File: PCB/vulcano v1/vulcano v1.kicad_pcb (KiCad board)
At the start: 2 copper layers, 4 parts, among them J1 Screw_Terminal_01x02, J2 Screw_Terminal_01x02, J3 conector t, U1 DOIT-ESP32-DEVKIT-V1

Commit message: placa principal
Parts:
- added A1: Arduino_UNO_R2, Module:Arduino_UNO_R2, B.Cu at (210.4, 77.6)
- added C1: 0.33uF, Capacitor_THT:C_Disc_D4.3mm_W1.9mm_P5.00mm, F.Cu at (49.7, 60.8)
- added C2: 0.1uF, Capacitor_THT:C_Disc_D4.3mm_W1.9mm_P5.00mm, F.Cu at (49.7, 72.9)
- added C3: 0.33uF, Capacitor_THT:C_Disc_D4.3mm_W1.9mm_P5.00mm, F.Cu at (58.6, 72.9)
- added C4: 0.1uF, Capacitor_THT:C_Disc_D4.3mm_W1.9mm_P5.00mm, F.Cu at (58.6, 60.7)
- added D1: 1N4007, Diode_THT:D_DO-41_SOD81_P10.16mm_Horizontal, F.Cu at (67.2, 77.1)
- added J4: Conn_02x05_Counter_Clockwise, Connector_IDC:IDC-Header_2x05_P2.54mm_Vertical, F.Cu at (138.1, 60.9)
- added J5: Conn_01x05_Pin, Connector_PinSocket_2.54mm:PinSocket_1x05_P2.54mm_Vertical, F.Cu at (117.2, 60.9)
- added J6: Conn_01x05_Pin, Connector_PinSocket_2.54mm:PinSocket_1x05_P2.54mm_Vertical, F.Cu at (121.1, 60.9)
- added J7: Conn_01x06_Pin, Connector_PinSocket_2.54mm:PinSocket_1x06_P2.54mm_Vertical, F.Cu at (136.8, 44.8)
- added J8: Conn_01x06_Pin, Connector_PinSocket_2.54mm:PinSocket_1x06_P2.54mm_Vertical, F.Cu at (136.8, 50.8)
- added Q1: BC547, Package_TO_SOT_THT:TO-92_Wide, F.Cu at (119.7, 68.8)
- added Q2: BC547, Package_TO_SOT_THT:TO-92_Wide, F.Cu at (131.7, 80.9)
- added Q3: BC547, Package_TO_SOT_THT:TO-92_Wide, F.Cu at (131.4, 67.4)
- added Q4: BC547, Package_TO_SOT_THT:TO-92_Wide, F.Cu at (116.2, 44.7)
- added Q5: BC547, Package_TO_SOT_THT:TO-92_Wide, F.Cu at (119.7, 81.3)
- added R12: 4k7, Resistor_THT:R_Axial_DIN0204_L3.6mm_D1.6mm_P7.62mm_Horizontal, F.Cu at (127.5, 45.0)
- added R15: 4k7, Resistor_THT:R_Axial_DIN0204_L3.6mm_D1.6mm_P7.62mm_Horizontal, F.Cu at (121.7, 87.8)
- added R3: 4k7, Resistor_THT:R_Axial_DIN0204_L3.6mm_D1.6mm_P7.62mm_Horizontal, F.Cu at (121.6, 74.0)
- added R6: 4k7, Resistor_THT:R_Axial_DIN0204_L3.6mm_D1.6mm_P7.62mm_Horizontal, F.Cu at (136.8, 86.4)
- added R9: 4k7, Resistor_THT:R_Axial_DIN0204_L3.6mm_D1.6mm_P7.62mm_Horizontal, F.Cu at (136.4, 73.5)
- added SW1: SW_SPDT, Button_Switch_THT:SW_CuK_JS202011CQN_DPDT_Straight, F.Cu at (69.5, 60.7)
- added U2: LM7809_TO220, Package_TO_SOT_THT:TO-220-3_Vertical, F.Cu at (53.6, 64.3)
- added U3: LM7806_TO220, Package_TO_SOT_THT:TO-220-3_Vertical, F.Cu at (64.0, 69.3)
- J1: footprint Connector_AMASS:AMASS_XT60-F_1x02_P7.20mm_Vertical -> TerminalBlock:TerminalBlock_bornier-2_P5.08mm
- J2: moved to F.Cu
- J3: value conector t -> Screw_Terminal_01x02; footprint Connector_AMASS:AMASS_XT60-F_1x02_P7.20mm_Vertical -> TerminalBlock:TerminalBlock_bornier-2_P5.08mm
- moved J2 129.6 mm to (60.0, 53.9), turned to 180 degrees
- moved J1 98.9 mm to (74.5, 53.8), turned to 180 degrees
- moved J3 91.3 mm to (72.0, 69.5)
- moved U1 43.2 mm to (95.0, 48.3)
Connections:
- net Net-(J1-Pin_2) renamed +12V
- J1 pad 1: GND -> Net-(J1-Pin_1)
- J2 pad 2: VCC -> GND
- U1 pad 10: unconnected-(U1-GPIO27_ADC2-CH7_RTC-GPIO17-Pad10) -> PWMA
- U1 pad 11: unconnected-(U1-GPIO14_ADC2-CH6_HSPI-CLK_RTC-GPIO16-Pad11) -> BIN1
- U1 pad 17: unconnected-(U1-GND-Pad17) -> GND
- U1 pad 18: unconnected-(U1-VIN-Pad18) -> +5V
- U1 pad 19: unconnected-(U1-3V3-Pad19) -> +3.3V
- U1 pad 20: unconnected-(U1-GPIO6_SCK/CLK-Pad20) -> X_SHUT_2
- U1 pad 21: unconnected-(U1-GPIO7_SDO/SD0-Pad21) -> X_SHUT_1
- U1 pad 26: unconnected-(U1-GPIO4_ADC2-CH0_RTC-GPIO10-Pad26) -> SENSOR_5_PIN
- U1 pad 29: unconnected-(U1-GPIO5_VSPI-CS0-Pad29) -> SENSOR_2_PIN
- U1 pad 30: unconnected-(U1-GPIO18_VSPI-CLK-Pad30) -> SENSOR_1_PIN
- U1 pad 31: unconnected-(U1-GPIO19_VSPI-MISO-Pad31) -> SENSOR_3_PIN
- U1 pad 32: unconnected-(U1-GPIO21_I2C-SDA-Pad32) -> SDA
- U1 pad 35: unconnected-(U1-GPIO22_I2C-SCL-Pad35) -> SCL
- U1 pad 36: unconnected-(U1-GPIO23_VSPI-MOSI-Pad36) -> SENSOR_4_PIN
- U1 pad 6: unconnected-(U1-GPIO32_ADC1-CH4_RTC-GPIO9-Pad6) -> BIN2
- U1 pad 7: unconnected-(U1-GPIO33_ADC1-CH5_RTC-GPIO8-Pad7) -> AIN2
- U1 pad 8: unconnected-(U1-GPIO25_ADC2-CH8_DAC1_RTC-GPIO6-Pad8) -> AIN1
- U1 pad 9: unconnected-(U1-GPIO26_ADC2-CH9_DAC2_RTC-GPIO7-Pad9) -> PWMB
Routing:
- net GND: track 0.00 -> 461.8 mm, vias 0 -> 2
- net +5V: track 0.00 -> 305.7 mm, vias 0 -> 4
- net BIN1: track 0.00 -> 209.2 mm
- net PWMA: track 0.00 -> 194.2 mm
- net PWMB: track 0.00 -> 182.2 mm
- net AIN1: track 0.00 -> 171.1 mm
- net AIN2: track 0.00 -> 160.4 mm
- net BIN2: track 0.00 -> 148.7 mm
- net +3.3V: track 0.00 -> 127.7 mm
- net RX_1: track 0.00 -> 81.3 mm, vias 0 -> 2
- net X_SHUT_1: track 0.00 -> 64.0 mm, vias 0 -> 2
- net X_SHUT_2: track 0.00 -> 40.1 mm, vias 0 -> 2
- net +12V: track 0.00 -> 37.9 mm
- net Sensores: track 0.00 -> 36.4 mm
- net Sensores_2: track 0.00 -> 32.9 mm
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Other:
- board outline added: 180 x 80 mm

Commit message: pcb vulcano terminada (reviasala ana)
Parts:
- removed SW1: SW_SPDT, Button_Switch_THT:SW_CuK_JS202011CQN_DPDT_Straight
- added BZ1: Buzzer, Buzzer_Beeper:MagneticBuzzer_Kingstate_KCG0601, F.Cu at (100.6, 52.6)
- added C5: C_Polarized_US, Capacitor_THT:CP_Radial_D8.0mm_P5.00mm, F.Cu at (76.8, 52.8)
- added J10: Conn_01x03_Pin, Connector_PinHeader_2.54mm:PinHeader_1x03_P2.54mm_Vertical, F.Cu at (76.1, 81.3)
- added J11: Conn_01x06_Pin, Connector_PinHeader_2.54mm:PinHeader_1x06_P2.54mm_Vertical, F.Cu at (87.4, 46.7)
- added J9: Conn_01x05_Pin, Connector_PinHeader_2.54mm:PinHeader_1x05_P2.54mm_Vertical, F.Cu at (49.3, 81.4)
- added Q6: BC547, Package_TO_SOT_THT:TO-92_Wide, F.Cu at (102.4, 56.1)
- added R1: 4k7, Resistor_THT:R_Axial_DIN0204_L3.6mm_D1.6mm_P7.62mm_Horizontal, F.Cu at (177.3, 110.2)
- added R2: 4k7, Resistor_THT:R_Axial_DIN0204_L3.6mm_D1.6mm_P7.62mm_Horizontal, F.Cu at (105.0, 71.1)
- added REF**: MountingHole_3.2mm_M3, MountingHole:MountingHole_3.2mm_M3, F.Cu at (48.5, 42.0)
- added REF**: MountingHole_3.2mm_M3, MountingHole:MountingHole_3.2mm_M3, F.Cu at (209.2, 109.1)
- added SW2: SW_Push, Button_Switch_THT:SW_PUSH_6mm, F.Cu at (59.3, 101.3)
- J1, J3: footprint TerminalBlock:TerminalBlock_bornier-2_P5.08mm -> deans:DEANS
- J2: footprint Connector_AMASS:AMASS_XT60-F_1x02_P7.20mm_Vertical -> Connector_AMASS:AMASS_XT60-M_1x02_P7.20mm_Vertical
- moved J3 25.6 mm to (69.6, 44.0), turned to -90 degrees
- moved J1 7.48 mm to (70.4, 60.0), turned to -135 degrees
- moved Q4 3.34 mm to (115.2, 47.9)
- moved J2 3.07 mm to (57.0, 53.9), turned to 90 degrees
- moved R12 2.29 mm to (127.6, 47.3)
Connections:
- A1 pad 5: +5V -> +3.3V
- J1 pad 1: Net-(J1-Pin_1) -> VCC
- U1 pad 13: unconnected-(U1-GPIO13_ADC2-CH4_HSPI-MOSI_RTC-GPIO14-Pad13) -> DI
- U1 pad 14: unconnected-(U1-GPIO9_SHD/SD2-Pad14) -> SW
- U1 pad 15: unconnected-(U1-GPIO10_SWP/SD3-Pad15) -> DT
- U1 pad 16: unconnected-(U1-GPIO11_CSC/CMD-Pad16) -> CLK
- U1 pad 2: unconnected-(U1-GPIO36_ADC-CH0_SENS-VP_RTC-GPIO0-Pad2) -> CNY_1
- U1 pad 20: X_SHUT_2 -> unconnected-(U1-GPIO6_SCK/CLK-Pad20)
- U1 pad 22: unconnected-(U1-GPIO8_SDI/SD1-Pad22) -> X_SHUT_2
- U1 pad 25: unconnected-(U1-GPIO2_ADC2-CH2_RTC-GPIO12-Pad25) -> CNY_4
- U1 pad 28: unconnected-(U1-GPIO17_UART2-TX-Pad28) -> buzzer
- U1 pad 3: unconnected-(U1-GPIO39_ADC1-CH3_SENS-VN_RTC-GPIO3-Pad3) -> CNY_2
- U1 pad 4: unconnected-(U1-GPIO34_ADC1-CH6_RTC-GPIO4-Pad4) -> CNY_3
- U1 pad 5: unconnected-(U1-GPIO35_ADC1-CH7_RTC-GPIO5-Pad5) -> INIT
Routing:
- net +3.3V: track 127.7 -> 489.5 mm, vias 0 -> 4
- net INIT: track 0.00 -> 167.0 mm, vias 0 -> 2
- net GND: track 461.8 -> 553.8 mm
- net +5V: track 305.7 -> 224.7 mm, vias 4 -> 6
- net BIN1: track 209.2 -> 253.2 mm
- net CNY_4: track 0.00 -> 39.8 mm
- net SW: track 0.00 -> 34.1 mm, vias 0 -> 2
- net DT: track 0.00 -> 34.1 mm, vias 0 -> 2
- net CLK: track 0.00 -> 34.1 mm, vias 0 -> 2
- net CNY_3: track 0.00 -> 21.1 mm
- net CNY_2: track 0.00 -> 16.0 mm
- net VCC: track 8.77 -> 22.2 mm
- net CNY_1: track 0.00 -> 11.3 mm
- net Net-(BZ1--): track 0.00 -> 10.8 mm
- net Net-(J1-Pin_1): track 10.3 -> 0.00 mm
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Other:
- board size 180 x 80 mm -> 170.8 x 76.5 mm

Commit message: pdf atemga
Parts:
- moved J9 2.20 mm to (50.5, 83.2)
- moved R9 1.73 mm to (136.4, 71.7)
- moved Q3 1.39 mm to (131.5, 66.0)
- moved Q5 1.32 mm to (119.6, 82.6)
- moved R12 1.23 mm to (127.6, 46.1)
- moved R6 0.66 mm to (136.8, 87.1)
- moved Q2 0.66 mm to (131.7, 81.6)
- moved J10 0.40 mm to (76.2, 80.9)
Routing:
- net GND: track 553.8 -> 534.7 mm
- net +3.3V: track 489.5 -> 472.7 mm
- net BIN1: track 253.2 -> 257.4 mm
- net BIN2: track 146.5 -> 142.7 mm
- net +5V: track 224.7 -> 221.5 mm
- net AIN2: track 157.0 -> 153.8 mm
- net AIN1: track 167.5 -> 165.1 mm
- net Sensores_3: track 13.3 -> 11.6 mm
- net RX: track 23.1 -> 21.6 mm
- net PWMB: track 176.8 -> 175.4 mm
- net INIT: track 167.0 -> 165.7 mm
- net Sensores: track 36.4 -> 35.2 mm
- net PWMA: track 187.4 -> 186.4 mm
- net VCC: track 22.2 -> 21.2 mm
- net SDA: track 15.5 -> 14.6 mm
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
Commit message: placa central lista
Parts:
- C5: footprint Capacitor_THT:CP_Radial_D8.0mm_P5.00mm -> Capacitor_THT:CP_Radial_D13.0mm_P5.00mm
- moved J2 9.43 mm to (53.4, 62.7)
- moved C1 9.08 mm to (50.0, 69.8)
- moved C2 9.08 mm to (50.0, 82.0)
- moved C3 9.08 mm to (58.9, 82.0)
- moved U3 9.08 mm to (64.3, 78.4)
- moved C4 9.08 mm to (58.9, 69.8)
- moved U2 9.08 mm to (53.9, 73.4)
- moved J9 7.63 mm to (50.0, 90.8)
- moved J1 6.78 mm to (69.9, 66.8), turned to -90 degrees
- moved C5 6.72 mm to (70.7, 55.6)
- moved J3 6.10 mm to (63.5, 44.0)
- moved D1 5.96 mm to (69.5, 82.6)
- moved SW2 2.78 mm to (60.0, 104.0)
- moved J10 1.41 mm to (77.6, 80.9)
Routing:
- net (no net): track 0.73 -> 25.6 mm
- net +5V: track 221.5 -> 235.4 mm
- net PWMA: track 186.4 -> 195.0 mm
- net GND: track 534.7 -> 540.6 mm
- net PWMB: track 175.4 -> 181.1 mm
- net +3.3V: track 472.7 -> 467.3 mm
- net VCC: track 21.2 -> 25.6 mm
- net BIN1: track 257.4 -> 261.5 mm
- net CLK: track 33.7 -> 37.7 mm
- net DT: track 33.7 -> 37.3 mm
- net SW: track 33.7 -> 37.3 mm
- net AIN1: track 165.1 -> 168.3 mm
- net +12V: track 31.9 -> 29.7 mm
- net DI: track 6.72 -> 4.90 mm
- net BIN2: track 142.7 -> 141.7 mm
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
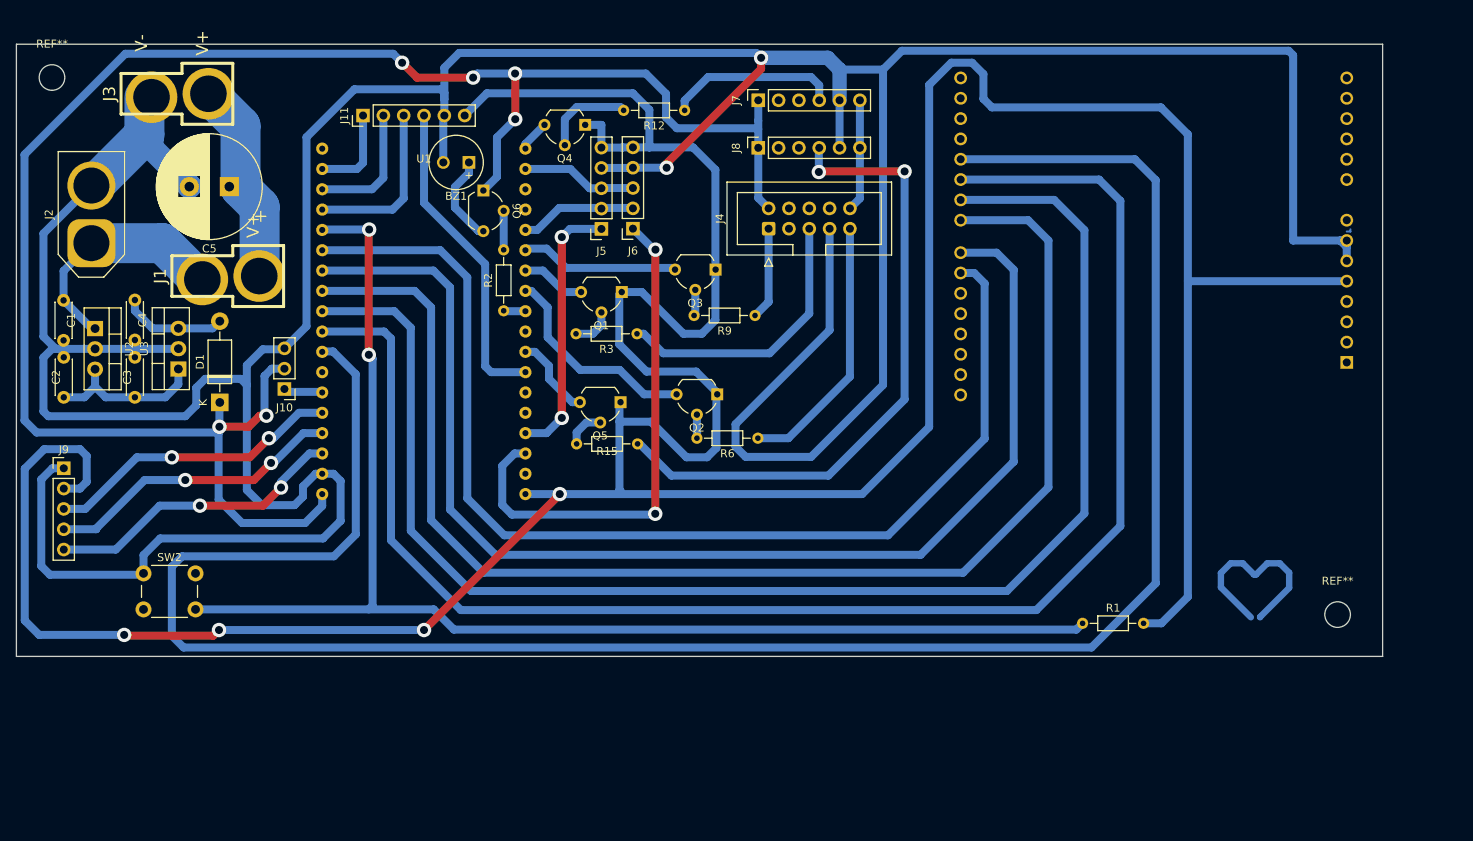
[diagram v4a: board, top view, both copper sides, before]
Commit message: placa vulcano falta indicar tornillos
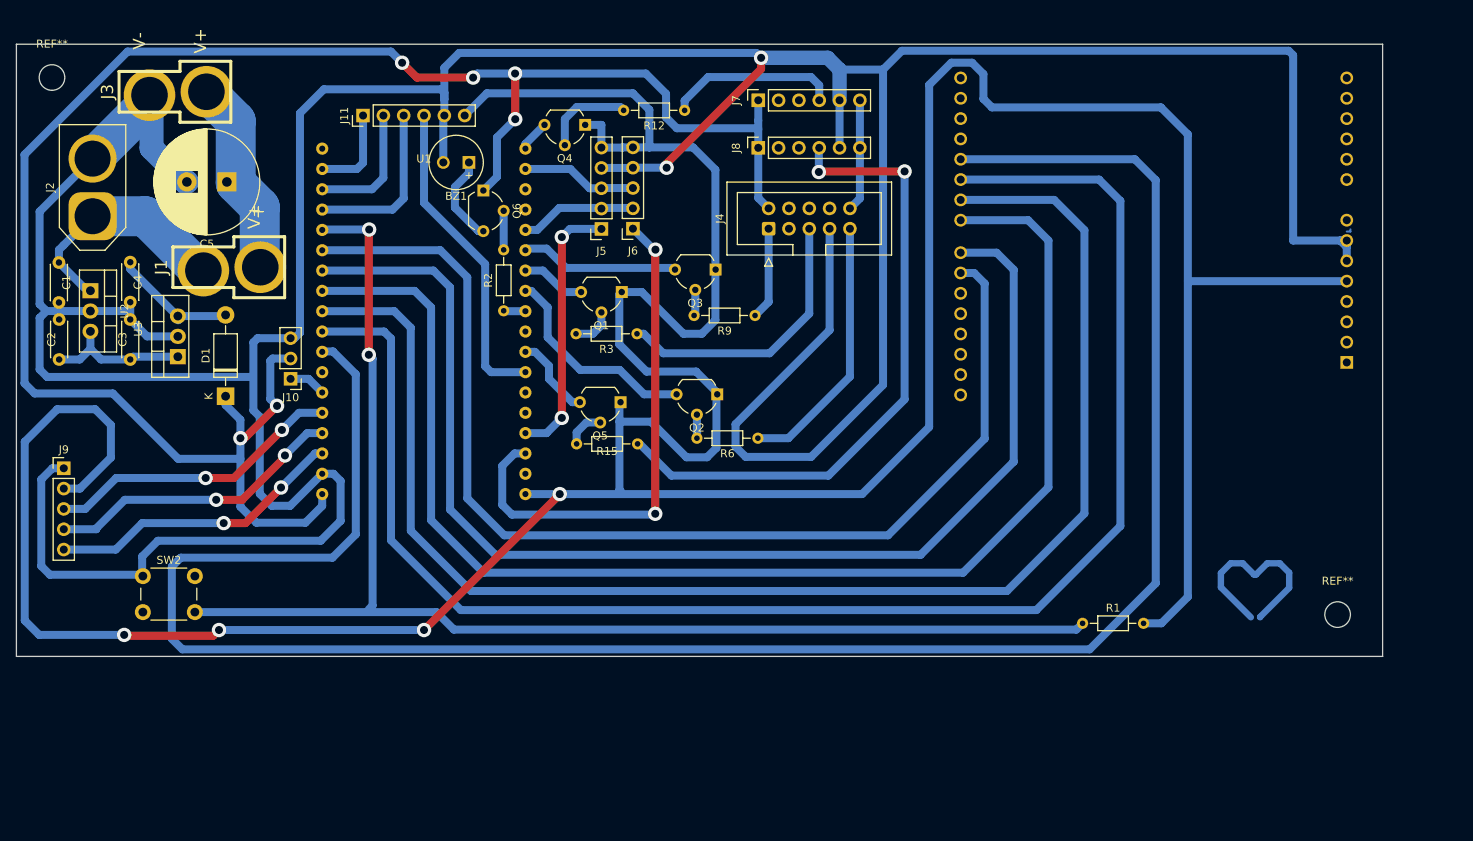
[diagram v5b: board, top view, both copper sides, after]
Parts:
- moved C1 4.76 mm to (49.4, 65.1)
- moved C2 4.76 mm to (49.4, 77.2)
- moved C3 4.76 mm to (58.3, 77.2)
- moved C4 4.76 mm to (58.3, 65.1)
- moved U2 4.76 mm to (53.3, 68.6)
- moved J2 3.37 mm to (53.6, 59.3)
- moved U3 1.54 mm to (64.3, 76.9)
- moved J10 1.49 mm to (78.3, 79.7)
- moved J1 1.11 mm to (70.0, 65.7)
- moved D1 1.06 mm to (70.2, 81.8)
- moved C5 0.66 mm to (70.4, 55.0)
- moved J3 0.36 mm to (63.2, 43.8)
- moved SW2 0.35 mm to (59.9, 104.3)
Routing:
- net +3.3V: track 467.3 -> 480.0 mm
- net GND: track 540.6 -> 534.2 mm
- net +6V: track 13.1 -> 16.2 mm
- net +9V: track 20.2 -> 18.3 mm
- net VCC: track 25.6 -> 24.8 mm
- net +5V: track 235.4 -> 235.9 mm
